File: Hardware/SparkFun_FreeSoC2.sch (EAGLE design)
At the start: 109 parts, among them U1 CY8C5888AXI-LP096, U2 MIC5219 5V, U3 MIC5219 3.3V, U4 2A/20V, U7 CY8C5868LTI-LP039, Y1 32.768kHz

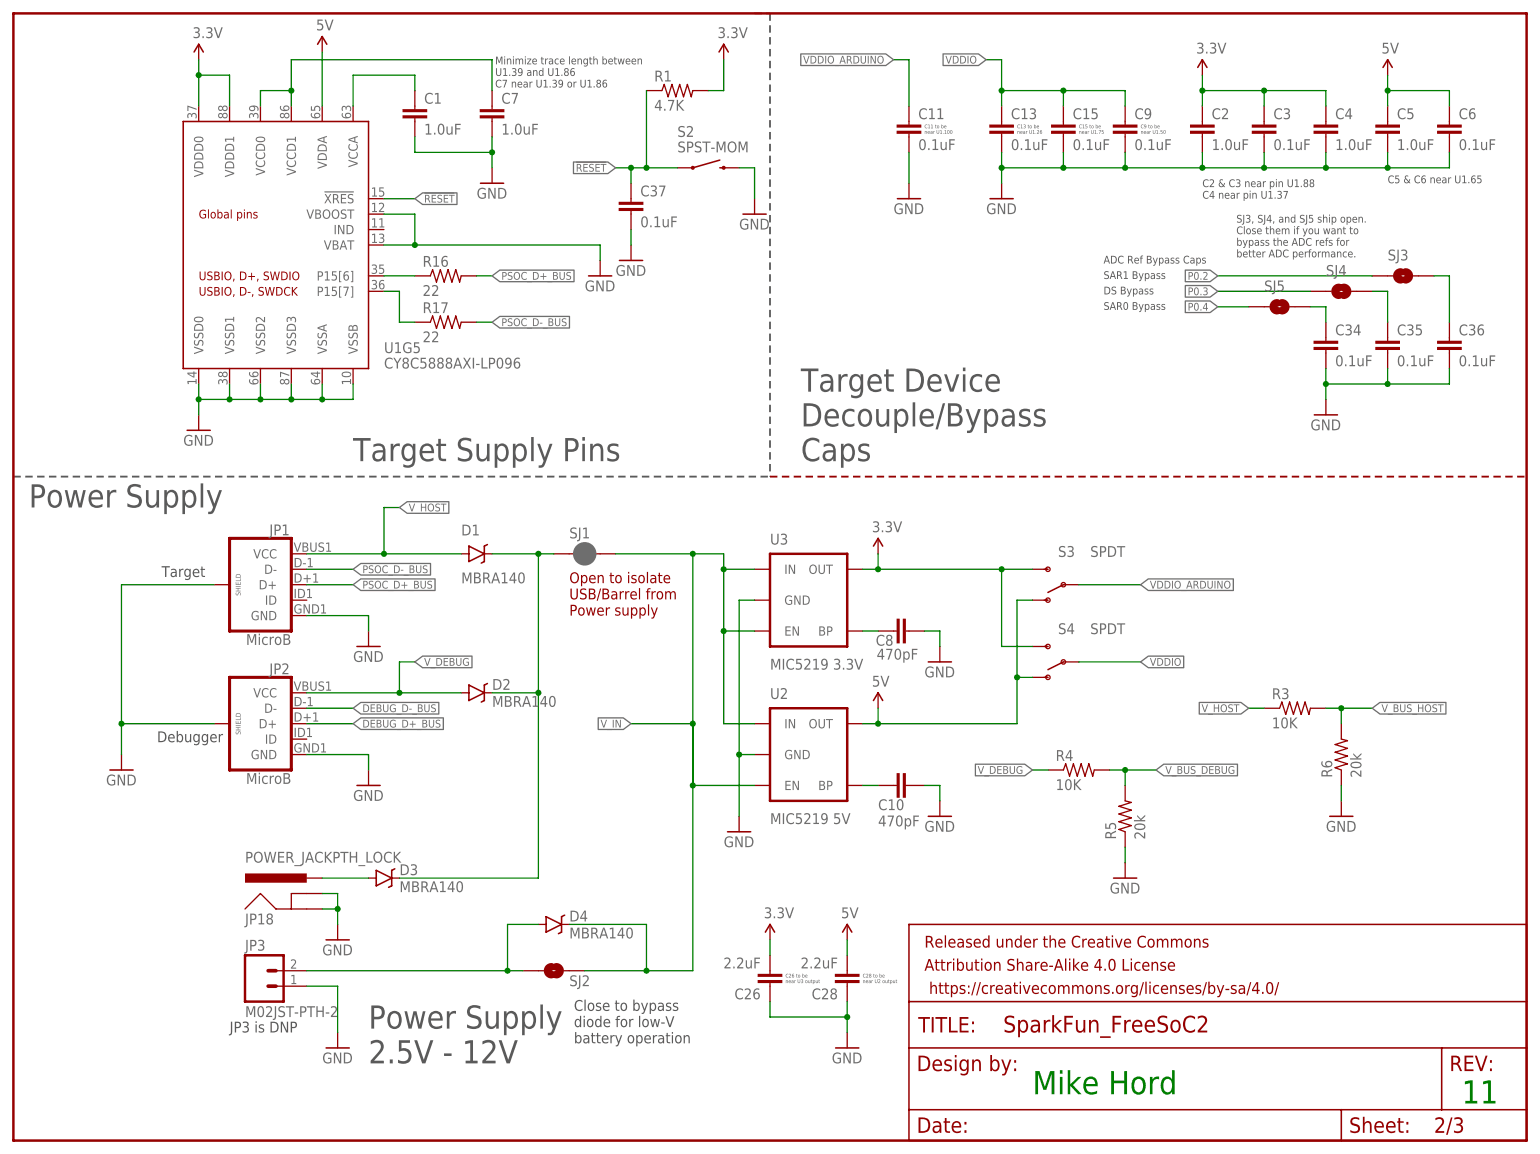
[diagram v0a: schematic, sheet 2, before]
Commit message: Rev to include changes from production
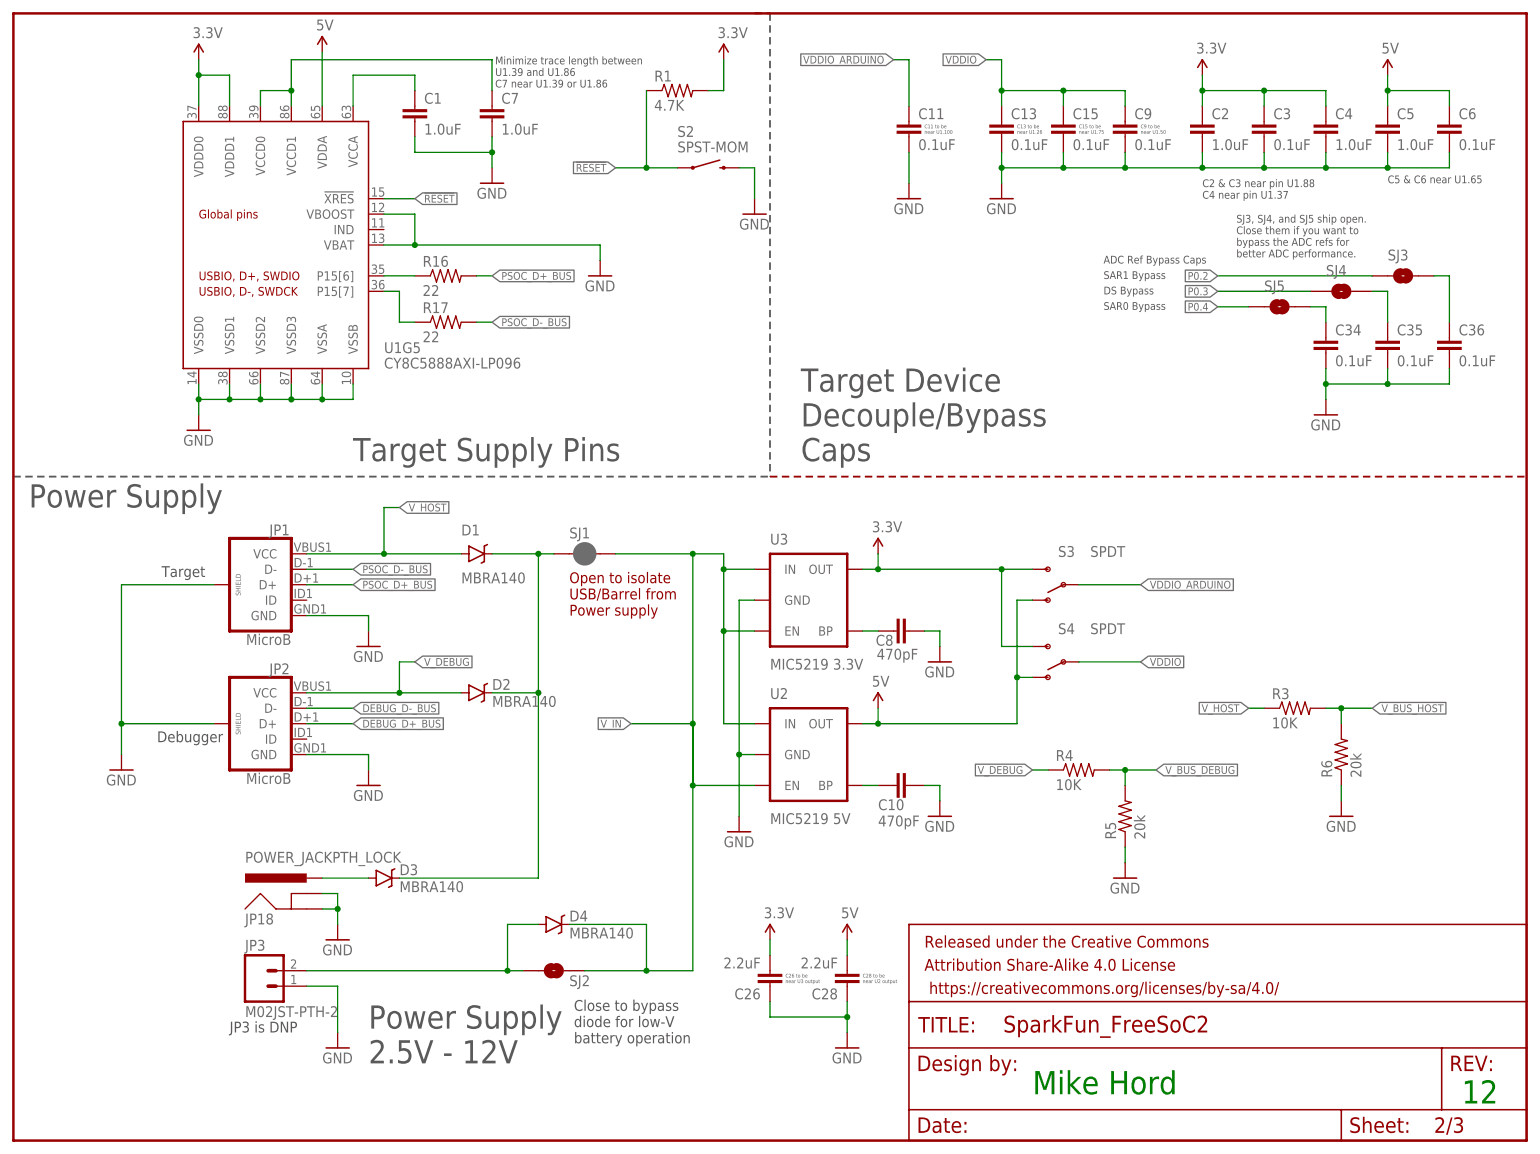
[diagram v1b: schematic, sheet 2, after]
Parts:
- removed C37, C38: 0.1uF, SparkFun-Capacitors:0.1UF-16V(+-10%)(0402)
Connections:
- net !DEBUG_RESET: no longer C38.1
- net !RESET: no longer C37.1
- net GND: no longer C37.2, C38.2
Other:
- note added: "12"
- note added: "ADC4, SDA"
- note added: "ADC5, SCL"
- note removed: "11"
- note removed: "ADC4, SCL"
- note removed: "ADC5, SDA"
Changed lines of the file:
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@@
 <part name="SUPPLY12" library="SparkFun-Aesthetics" deviceset="3.3V" device=""/>
 <part name="R1" library="SparkFun-Resistors" deviceset="4.7KOHM-1/10W-1%(0603)" device="" value="4.7K"/>
-<part name="C37" library="SparkFun-Capacitors" deviceset="0.1UF-16V(+-10%)(0402)" device="" value="0.1uF"/>
 <part name="SUPPLY13" library="SparkFun-Aesthetics" deviceset="3.3V" device=""/>
-<part name="GND34" library="SparkFun-Aesthetics" deviceset="GND" device=""/>
-<part name="C38" library="SparkFun-Capacitors" deviceset="0.1UF-16V(+-10%)(0402)" device="" value="0.1uF"/>
 <part name="R2" library="SparkFun-Resistors" deviceset="4.7KOHM-1/10W-1%(0603)" device="" value="4.7K"/>
 <part name="SUPPLY14" library="SparkFun-Aesthetics" deviceset="3.3V" device=""/>
 <part name="SUPPLY15" library="SparkFun-Aesthetics" deviceset="3.3V" device=""/>
 <part name="SUPPLY16" library="SparkFun-Aesthetics" deviceset="3.3V" device=""/>
-<part name="GND40" library="SparkFun-Aesthetics" deviceset="GND" device=""/>
 <part name="R3" library="SparkFun-Resistors" deviceset="10KOHM-1/10W-1%(0603)" device="0603" value="10K"/>
 <part name="R4" library="SparkFun-Resistors" deviceset="10KOHM-1/10W-1%(0603)" device="0603" value="10K"/>
@@
 <text x="165.1" y="127" size="1.27" layer="97" align="center-left">ADC0</text>
 <text x="165.1" y="129.54" size="1.27" layer="97" align="center-left">ADC1</text>
-<text x="165.1" y="154.94" size="1.27" layer="97" align="center-left">ADC5, SDA</text>
-<text x="165.1" y="152.4" size="1.27" layer="97" align="center-left">ADC4, SCL</text>
+<text x="165.1" y="154.94" size="1.27" layer="97" align="center-left">ADC5, SCL</text>
+<text x="165.1" y="152.4" size="1.27" layer="97" align="center-left">ADC4, SDA</text>
 <text x="165.1" y="147.32" size="1.27" layer="97" align="center-left">ADC2</text>
 <text x="165.1" y="149.86" size="1.27" layer="97" align="center-left">ADC3</text>
@@
 LED</text>
 <text x="167.64" y="7.62" size="3.81" layer="91">Mike Hord</text>
-<text x="238.76" y="6.096" size="3.81" layer="91">11</text>
+<text x="238.76" y="6.096" size="3.81" layer="91">12</text>
 </plain>
 <instances>
@@
 <text x="35.56" y="17.78" size="1.778" layer="97">JP3 is DNP</text>
 <text x="167.64" y="7.62" size="3.81" layer="91">Mike Hord</text>
-<text x="238.252" y="6.096" size="3.81" layer="91">11</text>
+<text x="238.252" y="6.096" size="3.81" layer="91">12</text>
 </plain>
 <instances>
@@
 <instance part="SUPPLY12" gate="G$1" x="195.58" y="175.26"/>
 <instance part="R1" gate="G$1" x="109.22" y="172.72"/>
-<instance part="C37" gate="G$1" x="101.6" y="152.4"/>
 <instance part="SUPPLY13" gate="G$1" x="116.84" y="177.8"/>
-<instance part="GND34" gate="1" x="101.6" y="144.78"/>
 <instance part="R3" gate="G$1" x="210.82" y="71.12"/>
 <instance part="R4" gate="G$1" x="175.26" y="60.96"/>
@@
 </segment>
 <segment>
-<pinref part="GND34" gate="1" pin="GND"/>
-<pinref part="C37" gate="G$1" pin="2"/>
-<wire x1="101.6" y1="147.32" x2="101.6" y2="149.86" width="0.1524" layer="91"/>
-</segment>
-<segment>
 <pinref part="R6" gate="G$1" pin="1"/>
 <pinref part="GND41" gate="1" pin="GND"/>
@@
 <wire x1="109.22" y1="160.02" x2="104.14" y2="160.02" width="0.1524" layer="91"/>
 <label x="99.06" y="160.02" size="1.27" layer="95" rot="R180" xref="yes"/>
-<pinref part="C37" gate="G$1" pin="1"/>
-<wire x1="104.14" y1="160.02" x2="101.6" y2="160.02" width="0.1524" layer="91"/>
-<wire x1="101.6" y1="160.02" x2="99.06" y2="160.02" width="0.1524" layer="91"/>
-<wire x1="101.6" y1="157.48" x2="101.6" y2="160.02" width="0.1524" layer="91"/>
-<junction x="101.6" y="160.02"/>
+<wire x1="104.14" y1="160.02" x2="99.06" y2="160.02" width="0.1524" layer="91"/>
 <pinref part="R1" gate="G$1" pin="1"/>
 <wire x1="104.14" y1="172.72" x2="104.14" y2="160.02" width="0.1524" layer="91"/>
@@
 to target via I2C</text>
 <text x="167.64" y="7.62" size="3.81" layer="91">Mike Hord</text>
-<text x="237.744" y="6.35" size="3.81" layer="91">11</text>
+<text x="237.744" y="6.35" size="3.81" layer="91">12</text>
 </plain>
 <instances>
@@
 <instance part="GND12" gate="1" x="233.68" y="99.06"/>
 <instance part="GND28" gate="1" x="43.18" y="142.24"/>
-<instance part="C38" gate="G$1" x="218.44" y="96.52"/>
 <instance part="R2" gate="G$1" x="223.52" y="114.3"/>
 <instance part="SUPPLY14" gate="G$1" x="231.14" y="116.84"/>
 <instance part="SUPPLY15" gate="G$1" x="170.18" y="175.26"/>
 <instance part="SUPPLY16" gate="G$1" x="53.34" y="27.94"/>
-<instance part="GND40" gate="1" x="218.44" y="88.9"/>
 <instance part="U4" gate="G1" x="38.1" y="45.72" smashed="yes" rot="MR180">
 <attribute name="NAME" x="38.862" y="42.926" size="1.778" layer="95" rot="MR180"/>
@@
 <pinref part="GND28" gate="1" pin="GND"/>
 </segment>
-<segment>
-<pinref part="GND40" gate="1" pin="GND"/>
-<pinref part="C38" gate="G$1" pin="2"/>
-<wire x1="218.44" y1="91.44" x2="218.44" y2="93.98" width="0.1524" layer="91"/>
-</segment>
 </net>
 <net name="N$14" class="0">
@@
 <segment>
 <pinref part="S1" gate="G$1" pin="1"/>
-<wire x1="220.98" y1="104.14" x2="218.44" y2="104.14" width="0.1524" layer="91"/>
 <label x="213.36" y="104.14" size="1.27" layer="95" rot="R180" xref="yes"/>
 <pinref part="R2" gate="G$1" pin="1"/>
-<wire x1="218.44" y1="104.14" x2="215.9" y2="104.14" width="0.1524" layer="91"/>
+<wire x1="220.98" y1="104.14" x2="215.9" y2="104.14" width="0.1524" layer="91"/>
 <wire x1="215.9" y1="104.14" x2="213.36" y2="104.14" width="0.1524" layer="91"/>
 <wire x1="218.44" y1="114.3" x2="215.9" y2="114.3" width="0.1524" layer="91"/>
 <wire x1="215.9" y1="114.3" x2="215.9" y2="104.14" width="0.1524" layer="91"/>
 <junction x="215.9" y="104.14"/>
-<pinref part="C38" gate="G$1" pin="1"/>
-<wire x1="218.44" y1="101.6" x2="218.44" y2="104.14" width="0.1524" layer="91"/>
-<junction x="218.44" y="104.14"/>
-</segment>
-</net>
+</segment>
+</net>

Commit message: Revisions from first production run
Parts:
- C18, C24: value 22pF -> (none); device SparkFun-Capacitors:22PF-50V-5%(0603) -> SparkFun-Capacitors:CAPPTH
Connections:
- net A4: now also JP7.9; no longer JP7.10
- net A5: now also JP7.10; no longer JP7.9
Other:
- note added: "Y2, C12 and C14 Y1, C18, and C24 are all DNP"
- note removed: "Y2, C12 and C14 are all DNP"
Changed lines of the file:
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@@
 <?xml version="1.0" encoding="utf-8"?>
 <!DOCTYPE eagle SYSTEM "eagle.dtd">
-<eagle version="7.1.0">
+<eagle version="7.3.0">
 <drawing>
 <settings>
@@
 <part name="C12" library="SparkFun-Capacitors" deviceset="CAP" device="PTH"/>
 <part name="C14" library="SparkFun-Capacitors" deviceset="CAP" device="PTH"/>
-<part name="C18" library="SparkFun-Capacitors" deviceset="22PF-50V-5%(0603)" device="" value="22pF"/>
-<part name="C24" library="SparkFun-Capacitors" deviceset="22PF-50V-5%(0603)" device="" value="22pF"/>
 <part name="Y1" library="SparkFun-FreqCtrl" deviceset="CRYSTAL" device="TC26H" value="32.768kHz"/>
 <part name="Y2" library="SparkFun-FreqCtrl" deviceset="CRYSTAL" device="HC49US"/>
@@
 <part name="FRAME2" library="SparkFun-Aesthetics" deviceset="FRAME-LETTER" device="NO_PACKAGE"/>
 <part name="FRAME3" library="SparkFun-Aesthetics" deviceset="FRAME-LETTER" device="NO_PACKAGE"/>
+<part name="C18" library="SparkFun-Capacitors" deviceset="CAP" device="PTH"/>
+<part name="C24" library="SparkFun-Capacitors" deviceset="CAP" device="PTH"/>
 </parts>
 <sheets>
@@
 <text x="165.1" y="134.62" size="1.27" layer="97" align="center-left">GPIO</text>
 <text x="165.1" y="165.1" size="1.27" layer="97" align="center-left">GPIO</text>
-<text x="225.806" y="54.356" size="1.27" layer="97">Y2, C12 and C14
+<text x="192.786" y="41.656" size="1.27" layer="97">Y2, C12 and C14
+Y1, C18, and C24
 are all DNP</text>
 <wire x1="147.32" y1="35.56" x2="111.76" y2="35.56" width="0.3048" layer="97" style="longdash"/>
@@
 <instance part="C12" gate="G$1" x="218.44" y="50.8"/>
 <instance part="C14" gate="G$1" x="208.28" y="50.8"/>
-<instance part="C18" gate="G$1" x="175.26" y="50.8"/>
-<instance part="C24" gate="G$1" x="190.5" y="50.8"/>
 <instance part="Y1" gate="G$1" x="182.88" y="60.96" smashed="yes" rot="R180">
 <attribute name="NAME" x="187.96" y="59.944" size="1.778" layer="95" rot="R180"/>
@@
 <instance part="FRAME3" gate="G$1" x="0" y="0"/>
 <instance part="FRAME3" gate="V" x="147.32" y="0"/>
+<instance part="C18" gate="G$1" x="175.26" y="50.8"/>
+<instance part="C24" gate="G$1" x="190.5" y="50.8"/>
 </instances>
 <busses>
@@
 <net name="A5" class="0">
 <segment>
+<pinref part="JP4" gate="G$1" pin="6"/>
+<wire x1="233.68" y1="162.56" x2="231.14" y2="162.56" width="0.1524" layer="91"/>
+<label x="231.14" y="162.56" size="1.27" layer="95" rot="R180" xref="yes"/>
+</segment>
+<segment>
+<pinref part="U1" gate="G3" pin="P6[0]"/>
+<wire x1="152.4" y1="154.94" x2="154.94" y2="154.94" width="0.1524" layer="91"/>
+<label x="154.94" y="154.94" size="1.27" layer="95" xref="yes"/>
+</segment>
+<segment>
+<pinref part="JP7" gate="G$1" pin="10"/>
+<wire x1="198.12" y1="121.92" x2="195.58" y2="121.92" width="0.1524" layer="91"/>
+<label x="195.58" y="121.92" size="1.27" layer="95" rot="R180" xref="yes"/>
+</segment>
+</net>
+<net name="A4" class="0">
+<segment>
+<pinref part="JP4" gate="G$1" pin="5"/>
+<wire x1="233.68" y1="165.1" x2="231.14" y2="165.1" width="0.1524" layer="91"/>
+<label x="231.14" y="165.1" size="1.27" layer="95" rot="R180" xref="yes"/>
+</segment>
+<segment>
+<pinref part="U1" gate="G3" pin="P6[1]"/>
+<wire x1="152.4" y1="152.4" x2="154.94" y2="152.4" width="0.1524" layer="91"/>
+<label x="154.94" y="152.4" size="1.27" layer="95" xref="yes"/>
+</segment>
+<segment>
 <pinref part="JP7" gate="G$1" pin="9"/>
 <wire x1="198.12" y1="124.46" x2="195.58" y2="124.46" width="0.1524" layer="91"/>
 <label x="195.58" y="124.46" size="1.27" layer="95" rot="R180" xref="yes"/>
-</segment>
-<segment>
-<pinref part="JP4" gate="G$1" pin="6"/>
-<wire x1="233.68" y1="162.56" x2="231.14" y2="162.56" width="0.1524" layer="91"/>
-<label x="231.14" y="162.56" size="1.27" layer="95" rot="R180" xref="yes"/>
-</segment>
-<segment>
-<pinref part="U1" gate="G3" pin="P6[0]"/>
-<wire x1="152.4" y1="154.94" x2="154.94" y2="154.94" width="0.1524" layer="91"/>
-<label x="154.94" y="154.94" size="1.27" layer="95" xref="yes"/>
-</segment>
-</net>
-<net name="A4" class="0">
-<segment>
-<pinref part="JP7" gate="G$1" pin="10"/>
-<wire x1="198.12" y1="121.92" x2="195.58" y2="121.92" width="0.1524" layer="91"/>
-<label x="195.58" y="121.92" size="1.27" layer="95" rot="R180" xref="yes"/>
-</segment>
-<segment>
-<pinref part="JP4" gate="G$1" pin="5"/>
-<wire x1="233.68" y1="165.1" x2="231.14" y2="165.1" width="0.1524" layer="91"/>
-<label x="231.14" y="165.1" size="1.27" layer="95" rot="R180" xref="yes"/>
-</segment>
-<segment>
-<pinref part="U1" gate="G3" pin="P6[1]"/>
-<wire x1="152.4" y1="152.4" x2="154.94" y2="152.4" width="0.1524" layer="91"/>
-<label x="154.94" y="152.4" size="1.27" layer="95" xref="yes"/>
 </segment>
 </net>
@@
 </segment>
 <segment>
-<pinref part="C18" gate="G$1" pin="2"/>
 <wire x1="175.26" y1="48.26" x2="175.26" y2="45.72" width="0.1524" layer="91"/>
-<pinref part="C24" gate="G$1" pin="2"/>
 <wire x1="175.26" y1="45.72" x2="190.5" y2="45.72" width="0.1524" layer="91"/>
 <wire x1="190.5" y1="45.72" x2="190.5" y2="48.26" width="0.1524" layer="91"/>
@@
 <wire x1="175.26" y1="43.18" x2="175.26" y2="45.72" width="0.1524" layer="91"/>
 <junction x="175.26" y="45.72"/>
+<pinref part="C18" gate="G$1" pin="2"/>
+<pinref part="C24" gate="G$1" pin="2"/>
 </segment>
 <segment>
@@
 </segment>
 <segment>
-<pinref part="C18" gate="G$1" pin="1"/>
 <wire x1="175.26" y1="55.88" x2="175.26" y2="60.96" width="0.1524" layer="91"/>
 <wire x1="175.26" y1="60.96" x2="175.26" y2="68.58" width="0.1524" layer="91"/>
@@
 <wire x1="180.34" y1="60.96" x2="175.26" y2="60.96" width="0.1524" layer="91"/>
 <junction x="175.26" y="60.96"/>
+<pinref part="C18" gate="G$1" pin="1"/>
 </segment>
 </net>
@@
 </segment>
 <segment>
-<pinref part="C24" gate="G$1" pin="1"/>
 <wire x1="190.5" y1="60.96" x2="190.5" y2="55.88" width="0.1524" layer="91"/>
 <wire x1="190.5" y1="60.96" x2="193.04" y2="60.96" width="0.1524" layer="91"/>
@@
 <wire x1="185.42" y1="60.96" x2="190.5" y2="60.96" width="0.1524" layer="91"/>
 <junction x="190.5" y="60.96"/>
-</segment>
-</net>
+<pinref part="C24" gate="G$1" pin="1"/>
+</segment>
+</net>
